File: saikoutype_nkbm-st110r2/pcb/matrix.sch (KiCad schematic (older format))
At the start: 239 parts, among them K00 CHRY_MX, K02 CHRY_MX, K03 CHRY_MX, K04 CHRY_MX, K05 CHRY_MX, K06 CHRY_MX, K07 CHRY_MX, K08 CHRY_MX, K09 CHRY_MX, K0B CHRY_MX, K0C CHRY_MX, K0D CHRY_MX, K0E CHRY_MX, K10 CHRY_MX, K11 CHRY_MX, K12 CHRY_MX, K13 CHRY_MX, K14 CHRY_MX, K15 CHRY_MX, K16 CHRY_MX, K17 CHRY_MX, K18 CHRY_MX, K19 CHRY_MX, K1A CHRY_MX, K1B CHRY_MX, K1C CHRY_MX, K1D CHRY_MX, K1E CHRY_MX, K1E1 CHRY_MX, K20 CHRY_MX, K21 CHRY_MX, K22 CHRY_MX, K23 CHRY_MX, K24 CHRY_MX, K25 CHRY_MX, K26 CHRY_MX, K27 CHRY_MX, K28 CHRY_MX, K29 CHRY_MX, K2A CHRY_MX, K2B CHRY_MX, K2C CHRY_MX, K30 CHRY_MX, K31 CHRY_MX, K32 CHRY_MX, K33 CHRY_MX, K34 CHRY_MX, K35 CHRY_MX, K36 CHRY_MX, K37 CHRY_MX, K38 CHRY_MX, K39 CHRY_MX, K3A CHRY_MX, K3B CHRY_MX, K3C CHRY_MX, K3C1 CHRY_MX, K3E CHRY_MX, K3E1 CHRY_MX, K40 CHRY_MX, K401 CHRY_MX, K41 CHRY_MX, K42 CHRY_MX, K43 CHRY_MX, K44 CHRY_MX, K45 CHRY_MX, K46 CHRY_MX, K47 CHRY_MX, K48 CHRY_MX, K49 CHRY_MX, K4A CHRY_MX, K4B CHRY_MX, K4C CHRY_MX, K4D CHRY_MX, K4D2 CHRY_MX, K50 CHRY_MX, K51 CHRY_MX, K511 CHRY_MX, K52 CHRY_MX, K521 CHRY_MX, K53 CHRY_MX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

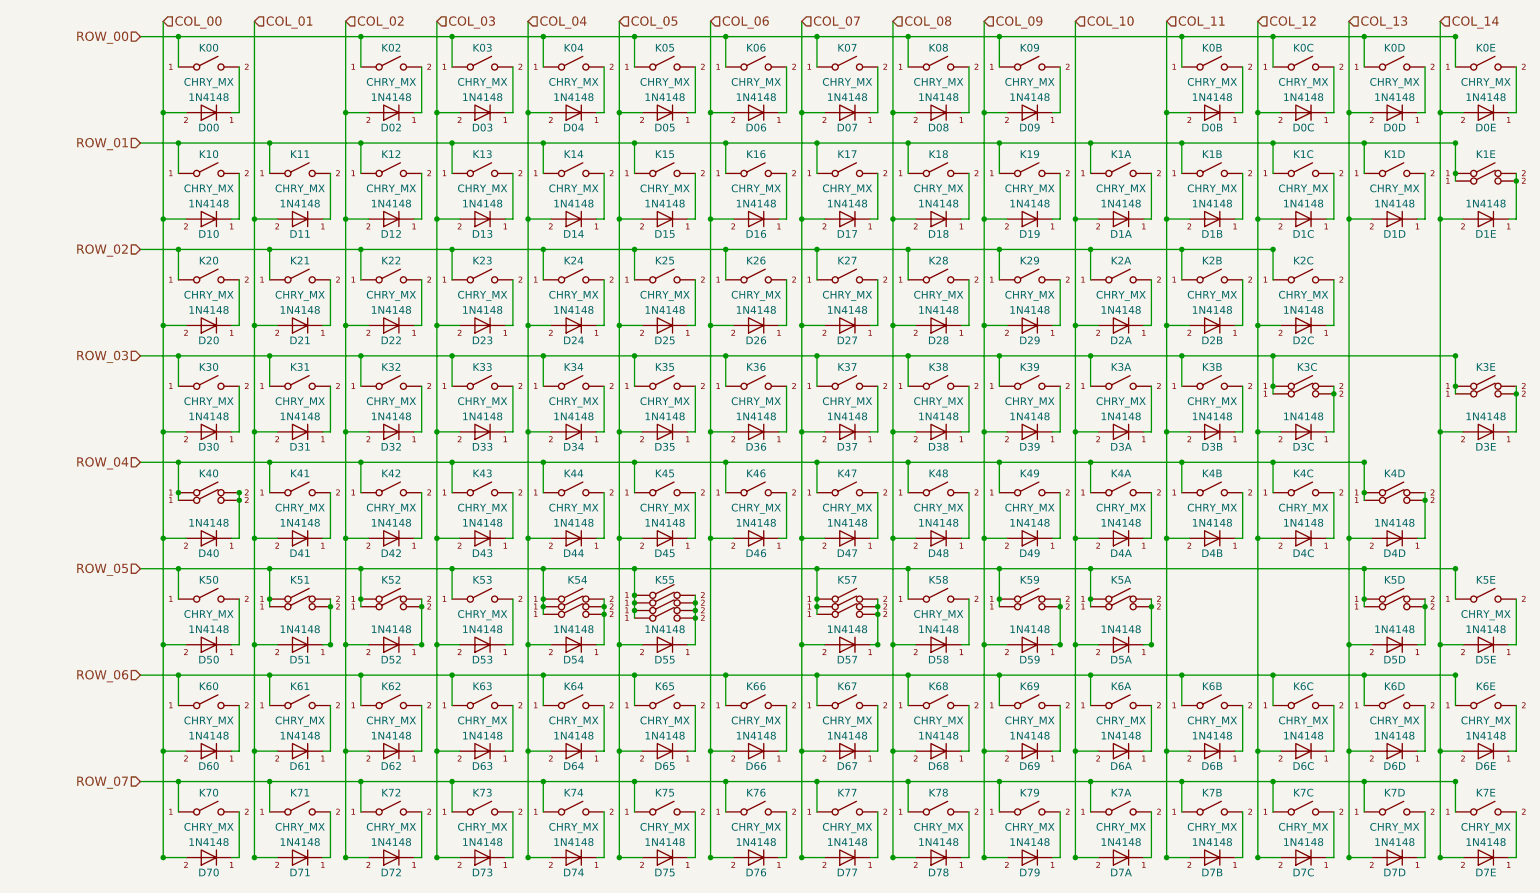
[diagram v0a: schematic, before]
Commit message: Fixed typo + updated schematic with graphics.
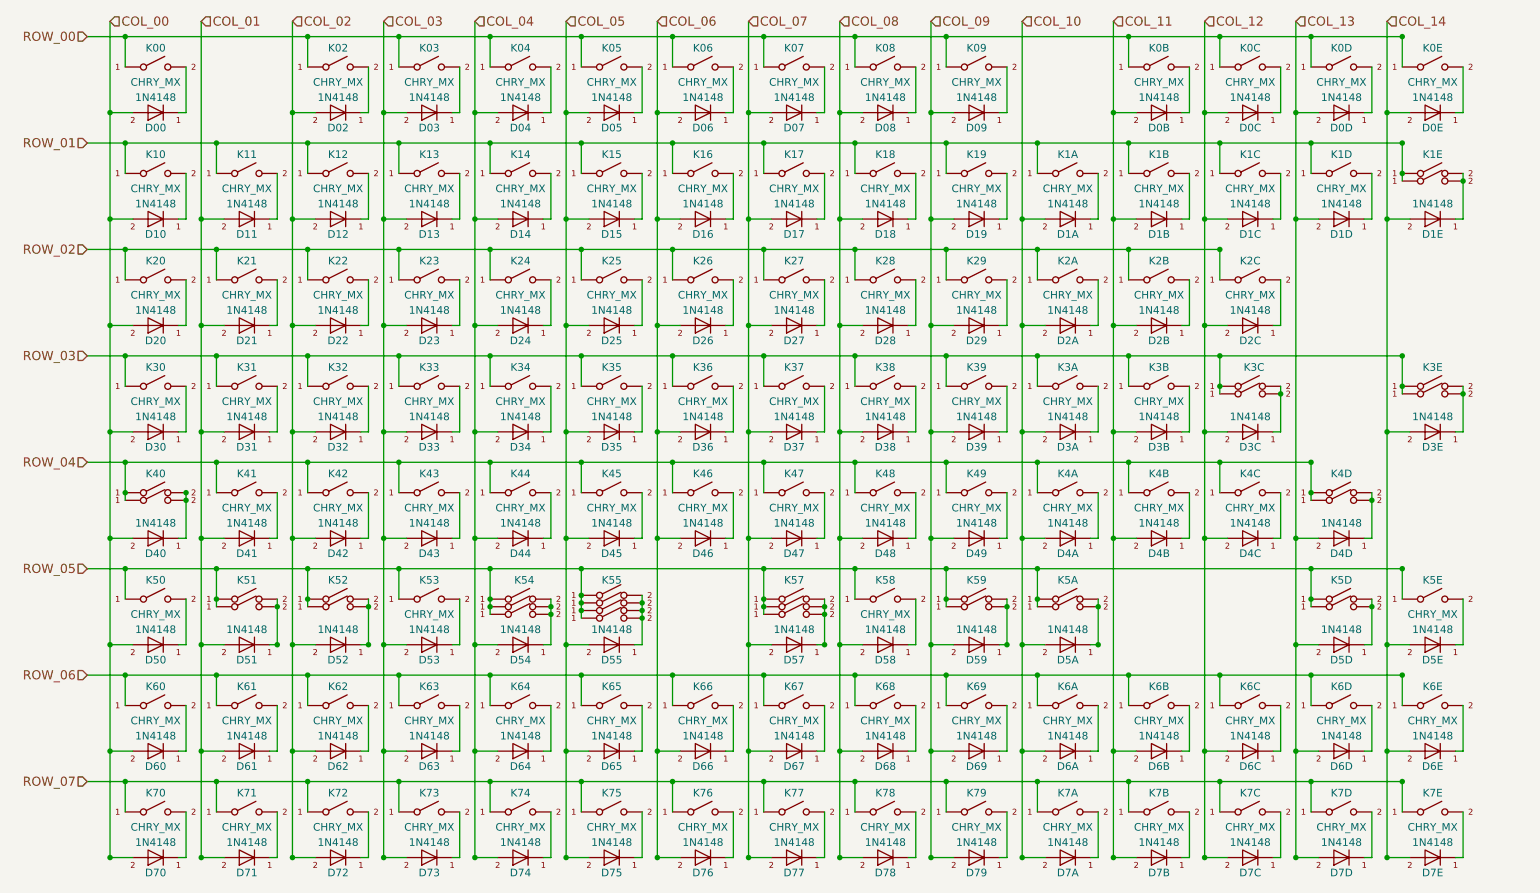
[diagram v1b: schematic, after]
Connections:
- new net: D3C.1 (K), K3C.~ (B), K3C1.~ (B)
- new net: D1E.1 (K), K1E.~ (B), K1E1.~ (B)
- new net: D40.1 (K), K40.~ (B), K401.~ (B)
- new net: D4D.1 (K), K4D.~ (B), K4D2.~ (B)
- new net: D51.1 (K), K51.~ (B), K511.~ (B)
- new net: D52.1 (K), K52.~ (B), K521.~ (B)
- new net: D54.1 (K), K54.~ (B), K541.~ (B), K542.~ (B)
- new net: D57.1 (K), K57.~ (B), K571.~ (B), K572.~ (B)
- new net: D55.1 (K), K55.~ (B), K551.~ (B), K552.~ (B), K553.~ (B)
- new net: D59.1 (K), K59.~ (B), K591.~ (B)
- new net: D5A.1 (K), K5A.~ (B), K5A1.~ (B)
- new net: D5D.1 (K), K5D.~ (B), K5D1.~ (B)
- new net: D3E.1 (K), K3E.~ (B), K3E1.~ (B)
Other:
- moved on the sheet: D00, D02, D03, D04, D05, D06, D07, D08, D09, D0B, D0C, D0D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

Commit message: Release NKBM-ST110 r2.1 2018.05.08
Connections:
- new net: D3C.1 (K), K3C.~ (B), K3C1.~ (B)
- new net: D1E.1 (K), K1E.~ (B), K1E1.~ (B)
- new net: D40.1 (K), K40.~ (B), K401.~ (B)
- new net: D4D.1 (K), K4D.~ (B), K4D2.~ (B)
- new net: D51.1 (K), K51.~ (B), K511.~ (B)
- new net: D52.1 (K), K52.~ (B), K521.~ (B)
- new net: D54.1 (K), K54.~ (B), K541.~ (B), K542.~ (B)
- new net: D57.1 (K), K57.~ (B), K571.~ (B), K572.~ (B)
- new net: D55.1 (K), K55.~ (B), K551.~ (B), K552.~ (B), K553.~ (B)
- new net: D59.1 (K), K59.~ (B), K591.~ (B)
- new net: D5A.1 (K), K5A.~ (B), K5A1.~ (B)
- new net: D5D.1 (K), K5D.~ (B), K5D1.~ (B)
- new net: D3E.1 (K), K3E.~ (B), K3E1.~ (B)
